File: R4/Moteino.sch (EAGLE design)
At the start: 21 parts, among them IC3 MCP1703CB, X1 16 MHz

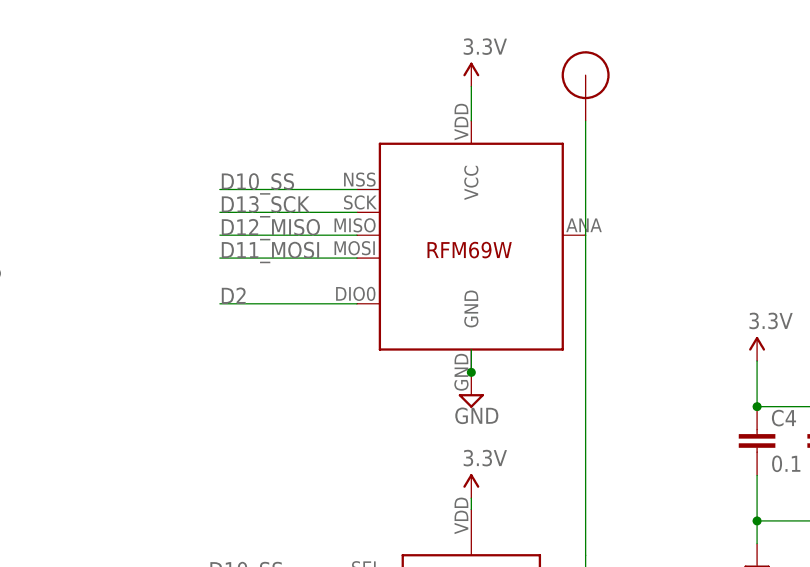
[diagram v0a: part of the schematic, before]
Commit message: Connect pin 3 with DIO2 https://github.com/kobuki/RFM69OOK
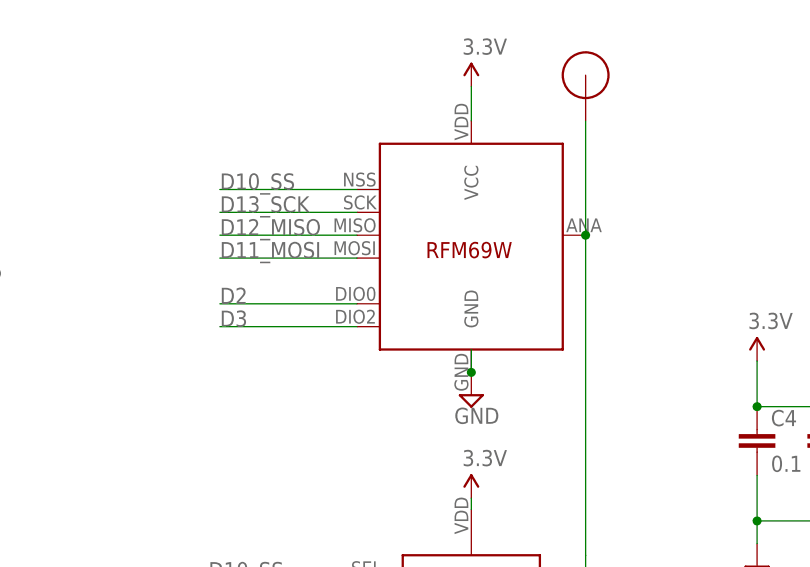
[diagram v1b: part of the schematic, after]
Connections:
- net D3: now also U$5.DIO2
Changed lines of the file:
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@@
 <?xml version="1.0" encoding="utf-8"?>
 <!DOCTYPE eagle SYSTEM "eagle.dtd">
-<eagle version="6.5.0">
+<eagle version="7.4.0">
 <drawing>
 <settings>
@@
 <setting verticaltext="up"/>
 </settings>
-<grid distance="0.1" unitdist="inch" unit="inch" style="lines" multiple="1" display="no" altdistance="0.01" altunitdist="inch" altunit="inch"/>
+<grid distance="0.05" unitdist="inch" unit="inch" style="lines" multiple="1" display="no" altdistance="0.01" altunitdist="inch" altunit="inch"/>
 <layers>
 <layer number="1" name="Top" color="4" fill="1" visible="no" active="no"/>
@@
 <layer number="54" name="bGND_GNDA" color="1" fill="9" visible="no" active="no"/>
 <layer number="56" name="wert" color="7" fill="1" visible="no" active="no"/>
+<layer number="90" name="Modules" color="5" fill="1" visible="yes" active="yes"/>
 <layer number="91" name="Nets" color="2" fill="1" visible="yes" active="yes"/>
 <layer number="92" name="Busses" color="1" fill="1" visible="yes" active="yes"/>
@@
 <label x="187.96" y="134.62" size="1.778" layer="95"/>
 </segment>
+<segment>
+<pinref part="U$5" gate="G$1" pin="DIO2"/>
+<wire x1="148.59" y1="80.01" x2="133.35" y2="80.01" width="0.1524" layer="91"/>
+<label x="133.35" y="80.01" size="1.778" layer="95"/>
+</segment>
 </net>
 <net name="D1_TX" class="0">
@@
 <wire x1="173.99" y1="46.99" x2="173.99" y2="54.61" width="0.1524" layer="91"/>
 <wire x1="173.99" y1="54.61" x2="173.99" y2="90.17" width="0.1524" layer="91"/>
-</segment>
-</net>
+<junction x="173.99" y="90.17"/>
+</segment>
+</net>

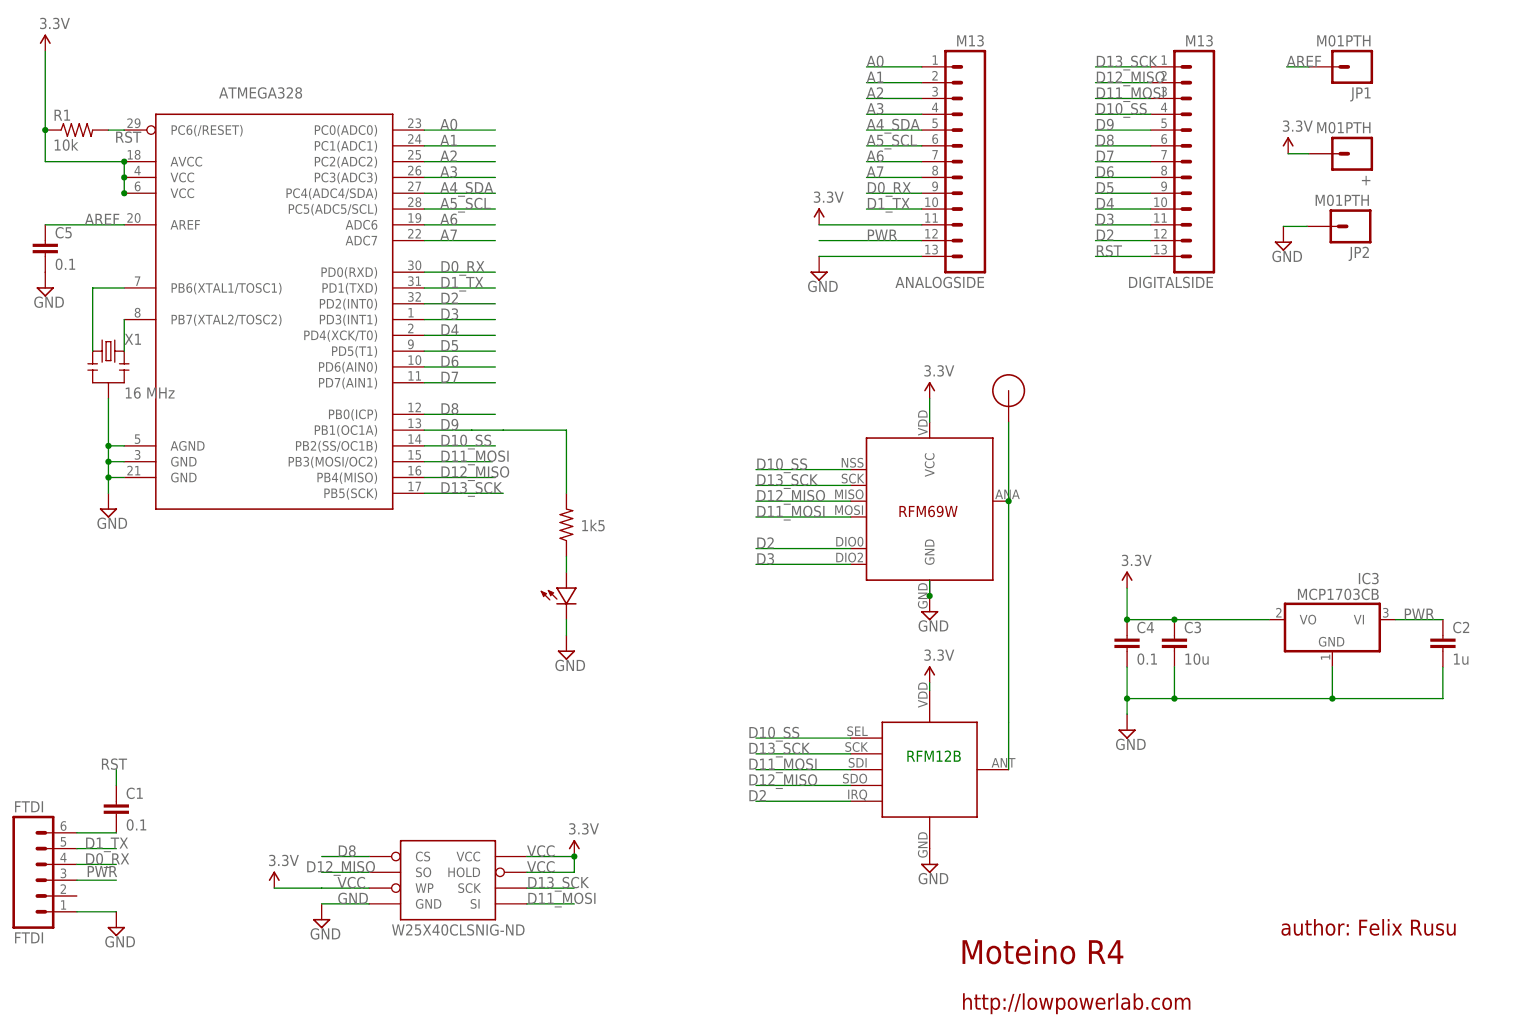
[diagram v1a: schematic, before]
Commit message: add capacitor values
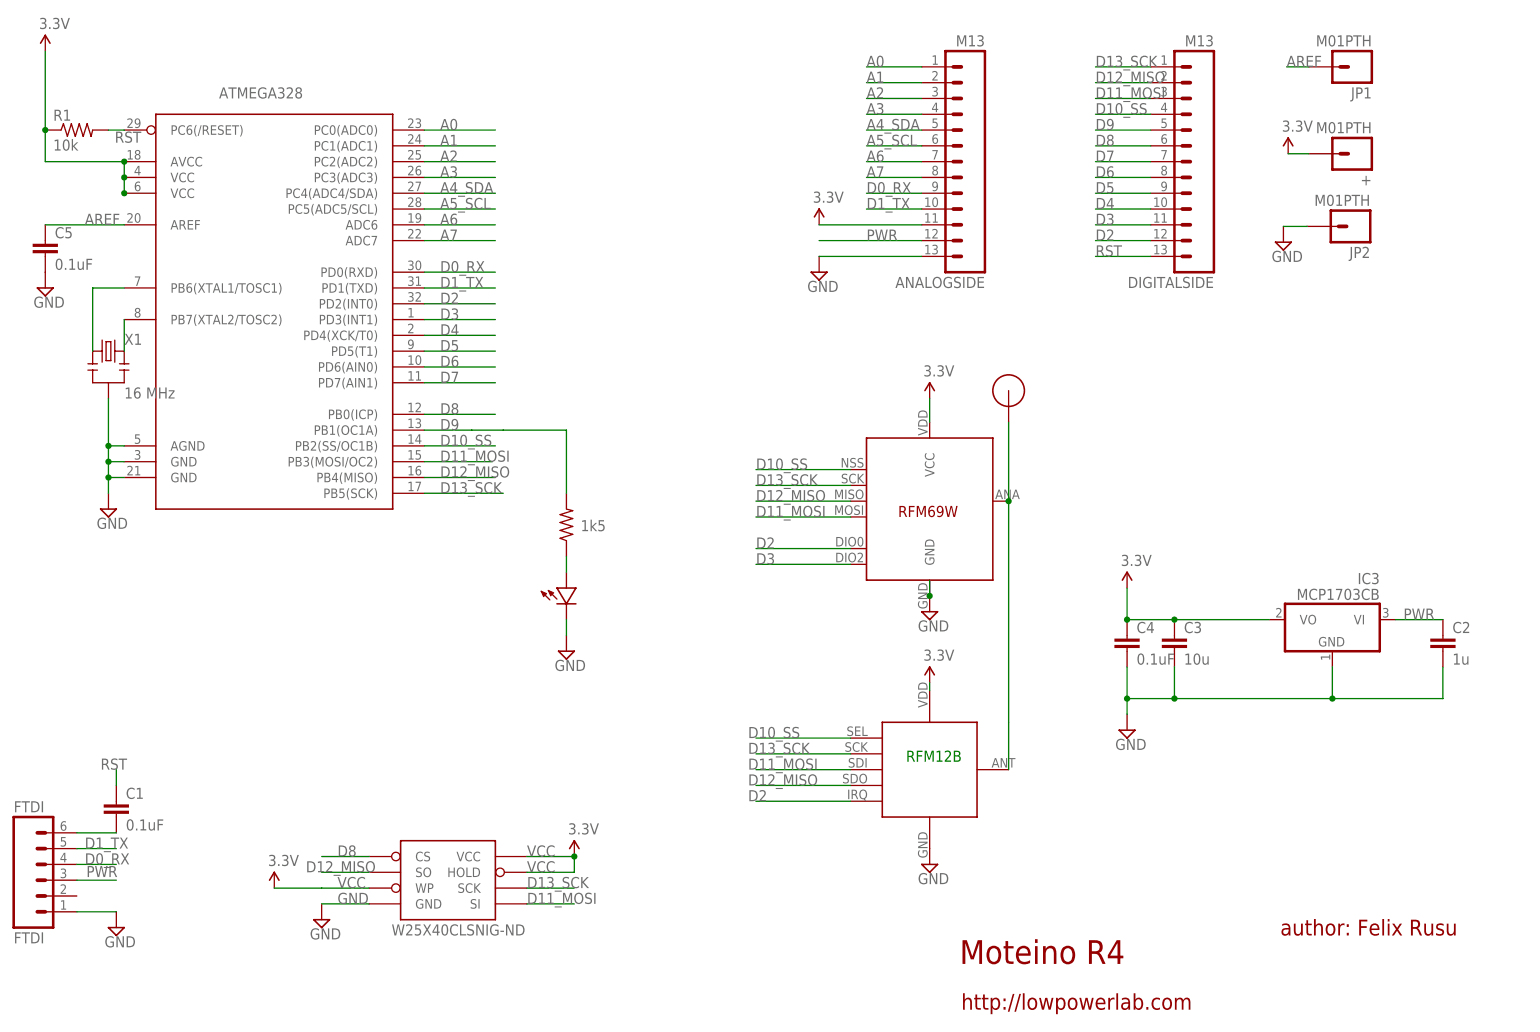
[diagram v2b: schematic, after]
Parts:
- C1, C4, C5: value 0.1 -> 0.1uF
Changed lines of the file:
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@@
 <setting verticaltext="up"/>
 </settings>
-<grid distance="0.05" unitdist="inch" unit="inch" style="lines" multiple="1" display="no" altdistance="0.01" altunitdist="inch" altunit="inch"/>
+<grid distance="0.1" unitdist="inch" unit="inch" style="lines" multiple="1" display="no" altdistance="0.01" altunitdist="inch" altunit="inch"/>
 <layers>
 <layer number="1" name="Top" color="4" fill="1" visible="no" active="no"/>
@@
 <part name="+" library="SparkFun-Connectors" deviceset="M01" device="PTH"/>
 <part name="P+3" library="SparkFun" deviceset="VCC" device="" value="3.3V"/>
-<part name="C5" library="LowPowerLab" deviceset="CAP" device="0603-CAP" value="0.1"/>
+<part name="C5" library="LowPowerLab" deviceset="CAP" device="0603-CAP" value="0.1uF"/>
 <part name="R1" library="LowPowerLab" deviceset="RESISTOR" device="0603-RES" value="10k"/>
-<part name="C1" library="LowPowerLab" deviceset="CAP" device="0603-CAP" value="0.1"/>
-<part name="C4" library="LowPowerLab" deviceset="CAP" device="0603-CAP" value="0.1"/>
+<part name="C1" library="LowPowerLab" deviceset="CAP" device="0603-CAP" value="0.1uF"/>
+<part name="C4" library="LowPowerLab" deviceset="CAP" device="0603-CAP" value="0.1uF"/>
 <part name="C2" library="LowPowerLab" deviceset="CAP" device="0603-CAP" value="1u"/>
 <part name="C3" library="LowPowerLab" deviceset="CAP" device="0805-CAP" value="10u"/>
